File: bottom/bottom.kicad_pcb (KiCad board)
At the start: 2 copper layers, 27.5 x 37.7 mm, 13 parts, among them P1 HLW4R-2C7LF, P2 BP167911-05340H0A

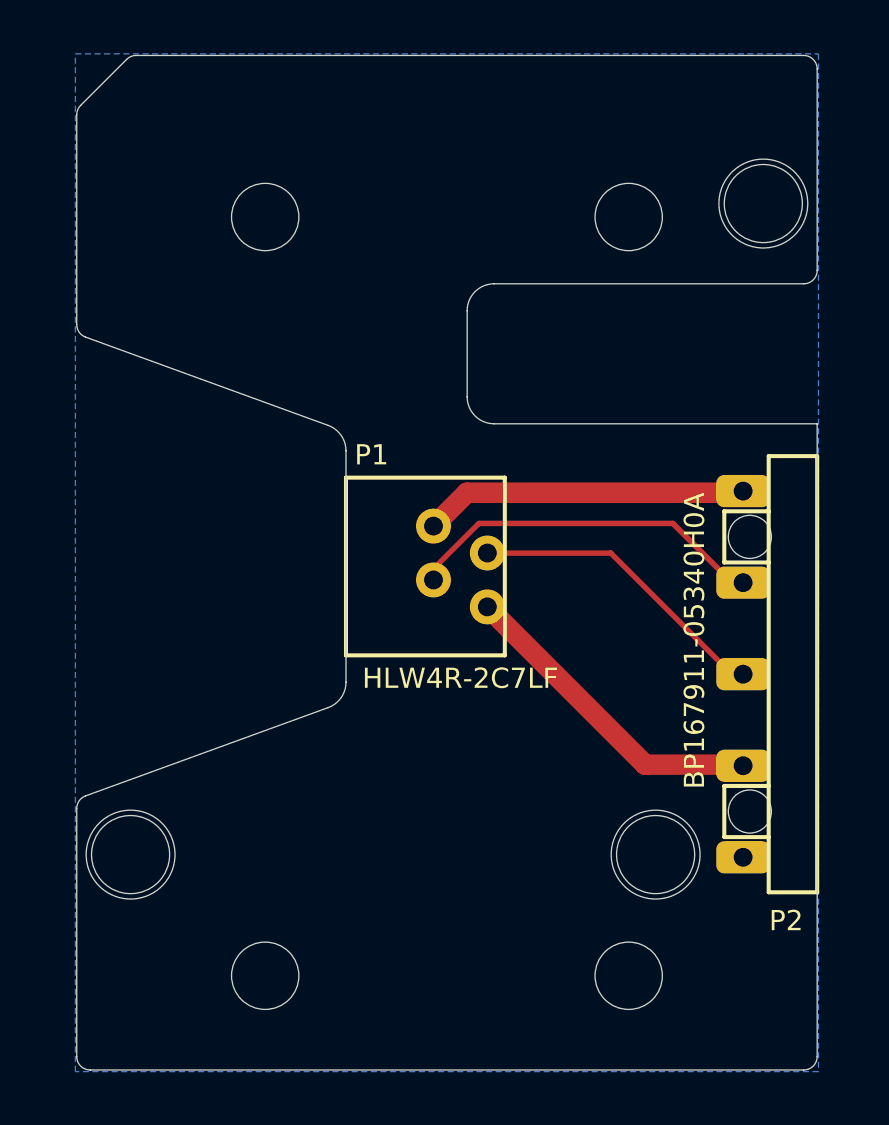
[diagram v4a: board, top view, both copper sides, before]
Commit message: Fix hole sizes and their keepout aeras.
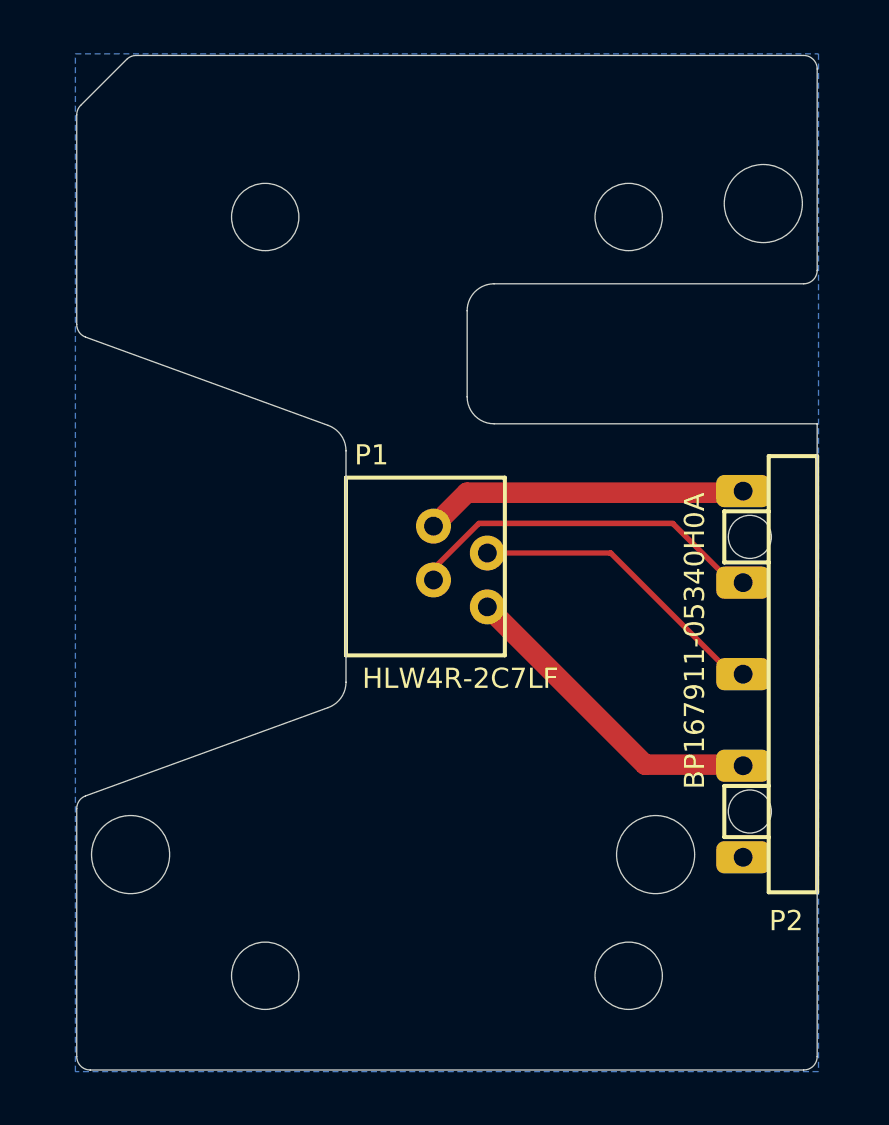
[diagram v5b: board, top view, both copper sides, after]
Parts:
- removed the ? at (219.3, 149.8)
- removed the ? at (199.8, 149.8)
- removed the ? at (223.3, 125.7)
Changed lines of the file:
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@@
-(kicad_pcb (version 20171130) (host pcbnew 5.1.3-ffb9f22~84~ubuntu18.04.1)
+(kicad_pcb (version 20171130) (host pcbnew 5.1.4-e60b266~84~ubuntu18.04.1)
   (general
     (thickness 1.6)
-    (drawings 33)
+    (drawings 58)
     (tracks 12)
     (zones 0)
-    (modules 13)
+    (modules 10)
     (nets 6)
   )
@@
       (clearance 0.00001))
   )
-  (module UGL:hole_3.2999999999999545mm locked (layer F.Cu)
-    (at 219.35 149.839996)
-    (attr virtual)
-    (fp_text reference "" (at 0 0) (layer F.SilkS)
-      (effects (font (size 1.27 1.27) (thickness 0.15)))
-    )
-    (fp_text value "" (at 0 0) (layer F.SilkS)
-      (effects (font (size 1.27 1.27) (thickness 0.15)))
-    )
-    (pad "" np_thru_hole circle (at 0 0) (size 3.3 3.3) (drill 3.3) (layers *.Cu *.Mask F.SilkS)
-      (clearance 0.00001))
-  )
-  (module UGL:hole_3.2999999999999545mm locked (layer F.Cu)
-    (at 199.85 149.839996)
-    (attr virtual)
-    (fp_text reference "" (at 0 0) (layer F.SilkS)
-      (effects (font (size 1.27 1.27) (thickness 0.15)))
-    )
-    (fp_text value "" (at 0 0) (layer F.SilkS)
-      (effects (font (size 1.27 1.27) (thickness 0.15)))
-    )
-    (pad "" np_thru_hole circle (at 0 0) (size 3.3 3.3) (drill 3.3) (layers *.Cu *.Mask F.SilkS)
-      (clearance 0.00001))
-  )
-  (module UGL:hole_3.3000000000000114mm locked (layer F.Cu)
-    (at 223.35 125.660004)
-    (attr virtual)
-    (fp_text reference "" (at 0 0) (layer F.SilkS)
-      (effects (font (size 1.27 1.27) (thickness 0.15)))
-    )
-    (fp_text value "" (at 0 0) (layer F.SilkS)
-      (effects (font (size 1.27 1.27) (thickness 0.15)))
-    )
-    (pad "" np_thru_hole circle (at 0 0) (size 3.3 3.3) (drill 3.3) (layers *.Cu *.Mask F.SilkS)
-      (clearance 0.00001))
-  )
   (module UGL:hole_2.5mm locked (layer F.Cu)
     (at 218.35 126.160004)
@@
       (clearance 0.00001))
   )
-  (gr_circle (center 223.35 125.660004) (end 223.35 127.310004) (layer Eco1.User) (width 0.01))
+  (gr_circle (center 199.85 149.839996) (end 201.5 149.839996) (layer Eco1.User) (width 0.01))
   (gr_text "PCB ID: touchpad_bottom_1.0.0" (at 212 156.8) (layer B.SilkS)
     (effects (font (size 0.75 0.75) (thickness 0.15)) (justify mirror))
@@
   (gr_arc (start 206.850001 143.43979) (end 207.19202 144.379485) (angle -70.00237317) (layer Edge.Cuts) (width 0.01))
   (gr_line (start 197.996447 122.013553) (end 199.703553 120.306447) (angle 90) (layer Edge.Cuts) (width 0.01))
-  (gr_circle (center 219.35 149.839996) (end 219.35 151.489996) (layer Eco1.User) (width 0.01))
-  (gr_circle (center 199.85 149.839996) (end 199.85 151.489996) (layer Eco1.User) (width 0.01))
   (gr_circle (center 204.85 154.339996) (end 206.75 154.339996) (layer Eco1.User) (width 0.01))
   (gr_circle (center 204.85 126.160004) (end 206.75 126.160004) (layer Eco1.User) (width 0.01))
   (gr_circle (center 218.35 126.160004) (end 220.25 126.160004) (layer Eco1.User) (width 0.01))
   (gr_circle (center 218.35 154.339996) (end 220.25 154.339996) (layer Eco1.User) (width 0.01))
+  (gr_circle (center 219.35 149.839996) (end 221 149.839996) (layer Eco1.User) (width 0.01))
+  (gr_circle (center 223.35 125.660004) (end 225 125.660004) (layer Eco1.User) (width 0.01))
+  (gr_arc (start 198.35 157.339989) (end 197.85 157.34) (angle -89.98521397) (layer Margin) (width 0.01))
+  (gr_arc (start 198.349992 148.129806) (end 198.17899 147.65996) (angle -70.01492042) (layer Margin) (width 0.01))
+  (gr_arc (start 224.85 157.339989) (end 224.85 157.84) (angle -90.00654586) (layer Margin) (width 0.01))
+  (gr_arc (start 224.850008 128.140007) (end 224.85 128.64) (angle -90.00660585) (layer Margin) (width 0.01))
+  (gr_arc (start 224.85 120.660011) (end 225.35 120.66) (angle -89.98521397) (layer Margin) (width 0.01))
+  (gr_arc (start 200.057104 120.659999) (end 200.057107 120.16) (angle -45.01451802) (layer Margin) (width 0.01))
+  (gr_arc (start 198.349988 122.367108) (end 197.996447 122.013553) (angle -45.04535319) (layer Margin) (width 0.01))
+  (gr_arc (start 198.349992 130.150193) (end 197.85 130.150194) (angle -69.99208089) (layer Margin) (width 0.01))
+  (gr_line (start 198.35 157.84) (end 224.85 157.84) (angle 90) (layer Margin) (width 0.01))
+  (gr_line (start 225.35 157.34) (end 225.35 133.84) (angle 90) (layer Margin) (width 0.01))
+  (gr_line (start 225.35 133.84) (end 213.35 133.84) (angle 90) (layer Margin) (width 0.01))
+  (gr_line (start 212.35 132.84) (end 212.35 129.64) (angle 90) (layer Margin) (width 0.01))
+  (gr_line (start 213.35 128.64) (end 224.85 128.64) (angle 90) (layer Margin) (width 0.01))
+  (gr_line (start 225.35 128.14) (end 225.35 120.66) (angle 90) (layer Margin) (width 0.01))
+  (gr_line (start 224.85 120.16) (end 200.057107 120.16) (angle 90) (layer Margin) (width 0.01))
+  (gr_line (start 197.85 122.367107) (end 197.85 130.150194) (angle 90) (layer Margin) (width 0.01))
+  (gr_line (start 197.85 148.129806) (end 197.85 157.34) (angle 90) (layer Margin) (width 0.01))
+  (gr_line (start 207.19202 144.379485) (end 198.17899 147.65996) (angle 90) (layer Margin) (width 0.01))
+  (gr_line (start 198.17899 130.62004) (end 207.19202 133.900515) (angle 90) (layer Margin) (width 0.01))
+  (gr_line (start 207.85 134.840208) (end 207.85 143.439792) (angle 90) (layer Margin) (width 0.01))
+  (gr_arc (start 213.349992 132.839997) (end 212.35 132.84) (angle -89.99574177) (layer Margin) (width 0.01))
+  (gr_arc (start 213.349999 129.639999) (end 213.35 128.64) (angle -90.00012957) (layer Margin) (width 0.01))
+  (gr_arc (start 206.850001 134.840209) (end 207.85 134.840208) (angle -69.99858612) (layer Margin) (width 0.01))
+  (gr_arc (start 206.850001 143.43979) (end 207.19202 144.379485) (angle -70.00237317) (layer Margin) (width 0.01))
+  (gr_line (start 197.996447 122.013553) (end 199.703553 120.306447) (angle 90) (layer Margin) (width 0.01))
   (segment (start 211.1 137.639999) (end 212.339999 136.4) (width 0.762) (layer F.Cu) (net 1))
   (segment (start 212.339999 136.4) (end 222.6 136.4) (width 0.762) (layer F.Cu) (net 1))

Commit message: Add hole clearances.
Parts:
- removed the ? at (219.3, 149.8)
- removed the ? at (199.8, 149.8)
- removed the ? at (223.3, 125.7)
- removed the ? at (204.8, 154.3)
- removed the ? at (204.8, 126.2)
- removed the ? at (218.3, 126.2)
- removed the ? at (218.3, 154.3)
- added ?: , ugl:hole_2.9mm, F.Cu at (219.3, 149.8)
- added ?: , ugl:hole_2.9mm, F.Cu at (199.8, 149.8)
- added ?: , ugl:hole_2.9mm, F.Cu at (223.3, 125.7)
- added ?: , ugl:hole_2.5mm, F.Cu at (204.8, 154.3)
- added ?: , ugl:hole_2.5mm, F.Cu at (204.8, 126.2)
- added ?: , ugl:hole_2.5mm, F.Cu at (218.3, 126.2)
- added ?: , ugl:hole_2.5mm, F.Cu at (218.3, 154.3)
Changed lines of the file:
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@@
     (add_net /VCC)
+  )
+  (module ugl:hole_2.9mm locked (layer F.Cu)
+    (at 219.35 149.839996)
+    (solder_mask_margin 0.2)
+    (clearance 0.2)
+    (attr virtual)
+    (fp_text reference "" (at 0 0) (layer F.SilkS)
+      (effects (font (size 1.27 1.27) (thickness 0.15)))
+    )
+    (fp_text value "" (at 0 0) (layer F.SilkS)
+      (effects (font (size 1.27 1.27) (thickness 0.15)))
+    )
+    (pad "" np_thru_hole circle (at 0 0) (size 2.9 2.9) (drill 2.9) (layers *.Cu *.Mask))
+  )
+  (module ugl:hole_2.9mm locked (layer F.Cu)
+    (at 199.85 149.839996)
+    (solder_mask_margin 0.2)
+    (clearance 0.2)
+    (attr virtual)
+    (fp_text reference "" (at 0 0) (layer F.SilkS)
+      (effects (font (size 1.27 1.27) (thickness 0.15)))
+    )
+    (fp_text value "" (at 0 0) (layer F.SilkS)
+      (effects (font (size 1.27 1.27) (thickness 0.15)))
+    )
+    (pad "" np_thru_hole circle (at 0 0) (size 2.9 2.9) (drill 2.9) (layers *.Cu *.Mask))
+  )
+  (module ugl:hole_2.9mm locked (layer F.Cu)
+    (at 223.35 125.660004)
+    (solder_mask_margin 0.2)
+    (clearance 0.2)
+    (attr virtual)
+    (fp_text reference "" (at 0 0) (layer F.SilkS)
+      (effects (font (size 1.27 1.27) (thickness 0.15)))
+    )
+    (fp_text value "" (at 0 0) (layer F.SilkS)
+      (effects (font (size 1.27 1.27) (thickness 0.15)))
+    )
+    (pad "" np_thru_hole circle (at 0 0) (size 2.9 2.9) (drill 2.9) (layers *.Cu *.Mask))
+  )
+  (module ugl:hole_2.5mm locked (layer F.Cu)
+    (at 204.85 154.339996)
+    (attr virtual)
+    (fp_text reference "" (at 0 0) (layer F.SilkS)
+      (effects (font (size 1.27 1.27) (thickness 0.15)))
+    )
+    (fp_text value "" (at 0 0) (layer F.SilkS)
+      (effects (font (size 1.27 1.27) (thickness 0.15)))
+    )
+    (pad "" np_thru_hole circle (at 0 0) (size 2.5 2.5) (drill 2.5) (layers *.Cu *.Mask))
+  )
+  (module ugl:hole_2.5mm locked (layer F.Cu)
+    (at 204.85 126.160004)
+    (attr virtual)
+    (fp_text reference "" (at 0 0) (layer F.SilkS)
+      (effects (font (size 1.27 1.27) (thickness 0.15)))
+    )
+    (fp_text value "" (at 0 0) (layer F.SilkS)
+      (effects (font (size 1.27 1.27) (thickness 0.15)))
+    )
+    (pad "" np_thru_hole circle (at 0 0) (size 2.5 2.5) (drill 2.5) (layers *.Cu *.Mask))
+  )
+  (module ugl:hole_2.5mm locked (layer F.Cu)
+    (at 218.35 126.160004)
+    (attr virtual)
+    (fp_text reference "" (at 0 0) (layer F.SilkS)
+      (effects (font (size 1.27 1.27) (thickness 0.15)))
+    )
+    (fp_text value "" (at 0 0) (layer F.SilkS)
+      (effects (font (size 1.27 1.27) (thickness 0.15)))
+    )
+    (pad "" np_thru_hole circle (at 0 0) (size 2.5 2.5) (drill 2.5) (layers *.Cu *.Mask))
+  )
+  (module ugl:hole_2.5mm locked (layer F.Cu)
+    (at 218.35 154.339996)
+    (attr virtual)
+    (fp_text reference "" (at 0 0) (layer F.SilkS)
+      (effects (font (size 1.27 1.27) (thickness 0.15)))
+    )
+    (fp_text value "" (at 0 0) (layer F.SilkS)
+      (effects (font (size 1.27 1.27) (thickness 0.15)))
+    )
+    (pad "" np_thru_hole circle (at 0 0) (size 2.5 2.5) (drill 2.5) (layers *.Cu *.Mask))
   )
   (module ugl:UHK_Logo_12x3.4_mm (layer B.Cu)
@@
       (net 1 /VCC) (clearance 0.0762))
   )
-  (module UGL:hole_2.8999999999999773mm locked (layer F.Cu)
-    (at 219.35 149.839996)
-    (attr virtual)
-    (fp_text reference "" (at 0 0) (layer F.SilkS)
-      (effects (font (size 1.27 1.27) (thickness 0.15)))
-    )
-    (fp_text value "" (at 0 0) (layer F.SilkS)
-      (effects (font (size 1.27 1.27) (thickness 0.15)))
-    )
-    (pad "" np_thru_hole circle (at 0 0) (size 2.9 2.9) (drill 2.9) (layers *.Cu *.Mask F.SilkS)
-      (clearance 0.00001))
-  )
-  (module UGL:hole_2.8999999999999773mm locked (layer F.Cu)
-    (at 199.85 149.839996)
-    (attr virtual)
-    (fp_text reference "" (at 0 0) (layer F.SilkS)
-      (effects (font (size 1.27 1.27) (thickness 0.15)))
-    )
-    (fp_text value "" (at 0 0) (layer F.SilkS)
-      (effects (font (size 1.27 1.27) (thickness 0.15)))
-    )
-    (pad "" np_thru_hole circle (at 0 0) (size 2.9 2.9) (drill 2.9) (layers *.Cu *.Mask F.SilkS)
-      (clearance 0.00001))
-  )
-  (module UGL:hole_2.9000000000000057mm locked (layer F.Cu)
-    (at 223.35 125.660004)
-    (attr virtual)
-    (fp_text reference "" (at 0 0) (layer F.SilkS)
-      (effects (font (size 1.27 1.27) (thickness 0.15)))
-    )
-    (fp_text value "" (at 0 0) (layer F.SilkS)
-      (effects (font (size 1.27 1.27) (thickness 0.15)))
-    )
-    (pad "" np_thru_hole circle (at 0 0) (size 2.9 2.9) (drill 2.9) (layers *.Cu *.Mask F.SilkS)
-      (clearance 0.00001))
-  )
-  (module UGL:hole_2.5mm locked (layer F.Cu)
-    (at 204.85 154.339996)
-    (attr virtual)
-    (fp_text reference "" (at 0 0) (layer F.SilkS)
-      (effects (font (size 1.27 1.27) (thickness 0.15)))
-    )
-    (fp_text value "" (at 0 0) (layer F.SilkS)
-      (effects (font (size 1.27 1.27) (thickness 0.15)))
-    )
-    (pad "" np_thru_hole circle (at 0 0) (size 2.5 2.5) (drill 2.5) (layers *.Cu *.Mask F.SilkS)
-      (clearance 0.00001))
-  )
-  (module UGL:hole_2.5mm locked (layer F.Cu)
-    (at 204.85 126.160004)
-    (attr virtual)
-    (fp_text reference "" (at 0 0) (layer F.SilkS)
-      (effects (font (size 1.27 1.27) (thickness 0.15)))
-    )
-    (fp_text value "" (at 0 0) (layer F.SilkS)
-      (effects (font (size 1.27 1.27) (thickness 0.15)))
-    )
-    (pad "" np_thru_hole circle (at 0 0) (size 2.5 2.5) (drill 2.5) (layers *.Cu *.Mask F.SilkS)
-      (clearance 0.00001))
-  )
-  (module UGL:hole_2.5mm locked (layer F.Cu)
-    (at 218.35 126.160004)
-    (attr virtual)
-    (fp_text reference "" (at 0 0) (layer F.SilkS)
-      (effects (font (size 1.27 1.27) (thickness 0.15)))
-    )
-    (fp_text value "" (at 0 0) (layer F.SilkS)
-      (effects (font (size 1.27 1.27) (thickness 0.15)))
-    )
-    (pad "" np_thru_hole circle (at 0 0) (size 2.5 2.5) (drill 2.5) (layers *.Cu *.Mask F.SilkS)
-      (clearance 0.00001))
-  )
-  (module UGL:hole_2.5mm locked (layer F.Cu)
-    (at 218.35 154.339996)
-    (attr virtual)
-    (fp_text reference "" (at 0 0) (layer F.SilkS)
-      (effects (font (size 1.27 1.27) (thickness 0.15)))
-    )
-    (fp_text value "" (at 0 0) (layer F.SilkS)
-      (effects (font (size 1.27 1.27) (thickness 0.15)))
-    )
-    (pad "" np_thru_hole circle (at 0 0) (size 2.5 2.5) (drill 2.5) (layers *.Cu *.Mask F.SilkS)
-      (clearance 0.00001))
-  )
   (gr_circle (center 199.85 149.839996) (end 201.5 149.839996) (layer Eco1.User) (width 0.01))

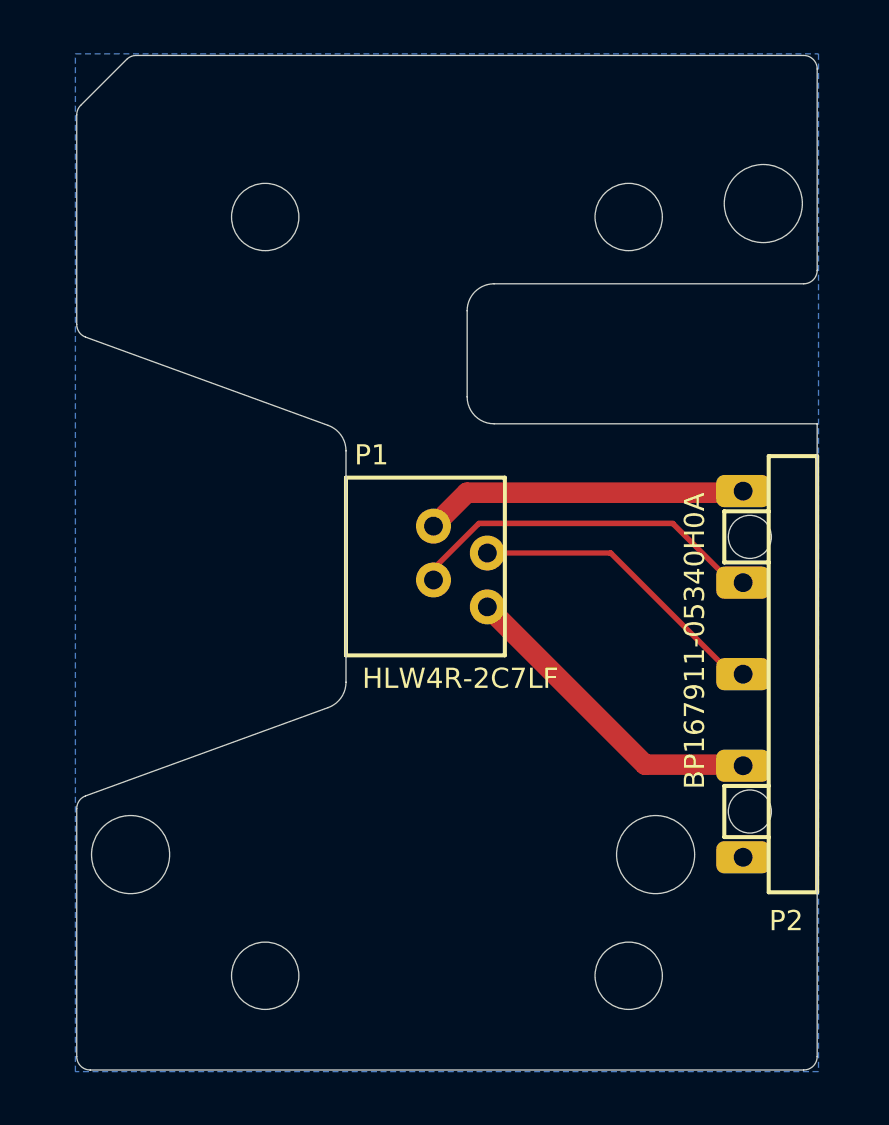
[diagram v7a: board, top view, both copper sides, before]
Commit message: Update bottom board based on CAD, and bump its version to 2.1.0
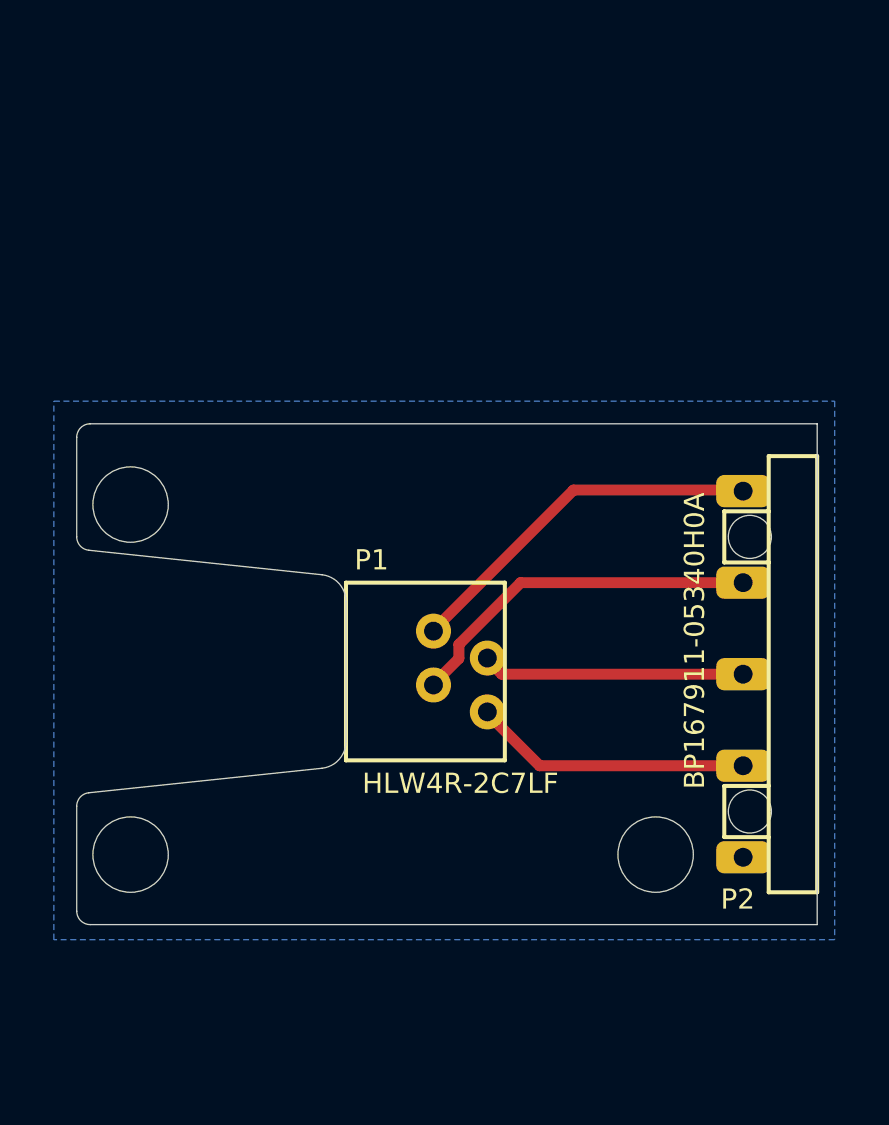
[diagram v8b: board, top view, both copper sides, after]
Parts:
- removed the ? at (219.3, 149.8)
- removed the ? at (199.8, 149.8)
- removed the ? at (223.3, 125.7)
- removed the ? at (204.8, 154.3)
- removed the ? at (204.8, 126.2)
- removed the ? at (218.3, 126.2)
- removed the ? at (218.3, 154.3)
- added ?: , ugl:hole_2.8mm, F.Cu at (219.3, 149.8)
- added ?: , ugl:hole_2.8mm, F.Cu at (199.8, 149.8)
- added ?: , ugl:hole_2.8mm, F.Cu at (199.8, 136.8)
- moved P1 3.90 mm to (207.8, 143.0)
- moved G*** 0.22 mm to (209.6, 149.7)
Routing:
- net /VCC: track 12.0 -> 13.7 mm
- net /GND: track 11.9 -> 10.3 mm
- net /SCL: track 11.4 -> 10.1 mm
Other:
- board size 27.5 x 37.7 mm -> 27.5 x 18.6 mm
- board text added: "PCB ID: touchpad_bottom_2.1.0"
- board text removed: "PCB ID: touchpad_bottom_1.0.0"
